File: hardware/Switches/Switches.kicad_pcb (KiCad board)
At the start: 2 copper layers, 22 parts, among them U101 MIC4604YM, U102 MIC4604YM

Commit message: snubber
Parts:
- added C105: 100n, Capacitor_SMD:C_1210_3225Metric_Pad1.33x2.70mm_HandSolder, F.Cu at (129.5, 71.5)
- added C106: 100n, Capacitor_SMD:C_1210_3225Metric_Pad1.33x2.70mm_HandSolder, F.Cu at (128.9, 97.8)
- added C107: 100n, Capacitor_SMD:C_1210_3225Metric_Pad1.33x2.70mm_HandSolder, F.Cu at (202.6, 70.2)
- added C108: 100n, Capacitor_SMD:C_1210_3225Metric_Pad1.33x2.70mm_HandSolder, F.Cu at (203.2, 97.8)
- added R109: 10, Resistor_SMD:R_1210_3225Metric_Pad1.30x2.65mm_HandSolder, F.Cu at (129.5, 65.7)
- added R110: 10, Resistor_SMD:R_1210_3225Metric_Pad1.30x2.65mm_HandSolder, F.Cu at (128.9, 92.4)
- added R111: 10, Resistor_SMD:R_1210_3225Metric_Pad1.30x2.65mm_HandSolder, F.Cu at (202.6, 64.8)
- added R112: 10, Resistor_SMD:R_1210_3225Metric_Pad1.30x2.65mm_HandSolder, F.Cu at (203.2, 92.1)
- moved R102 5.91 mm to (158.1, 81.3)
- moved R101 5.91 mm to (158.1, 78.7)
- moved C103 5.12 mm to (167.5, 84.8)
- moved U101 5.12 mm to (163.0, 84.8)
- moved C101 4.26 mm to (158.1, 83.8), turned to 180 degrees
- moved R105 1.75 mm to (158.2, 86.3)
- moved R106 1.75 mm to (158.2, 88.6)
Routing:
- net /SL1: track 2.07 -> 12.5 mm
- net /GH1_1: track 33.6 -> 28.0 mm
- net Net-(C101-Pad1): track 8.60 -> 5.32 mm
- net Net-(R105-Pad2): track 12.9 -> 9.76 mm
- net /GH1_2: track 20.8 -> 18.5 mm
- net /GL1_1: track 25.2 -> 23.0 mm
- net Net-(U101-Pad6): track 0.00 -> 1.85 mm, vias 0 -> 1
- net Net-(R101-Pad2): track 8.60 -> 7.26 mm
- net /GL1_2: track 33.0 -> 34.2 mm
- net Net-(U101-Pad5): track 0.65 -> 1.80 mm, vias 0 -> 1

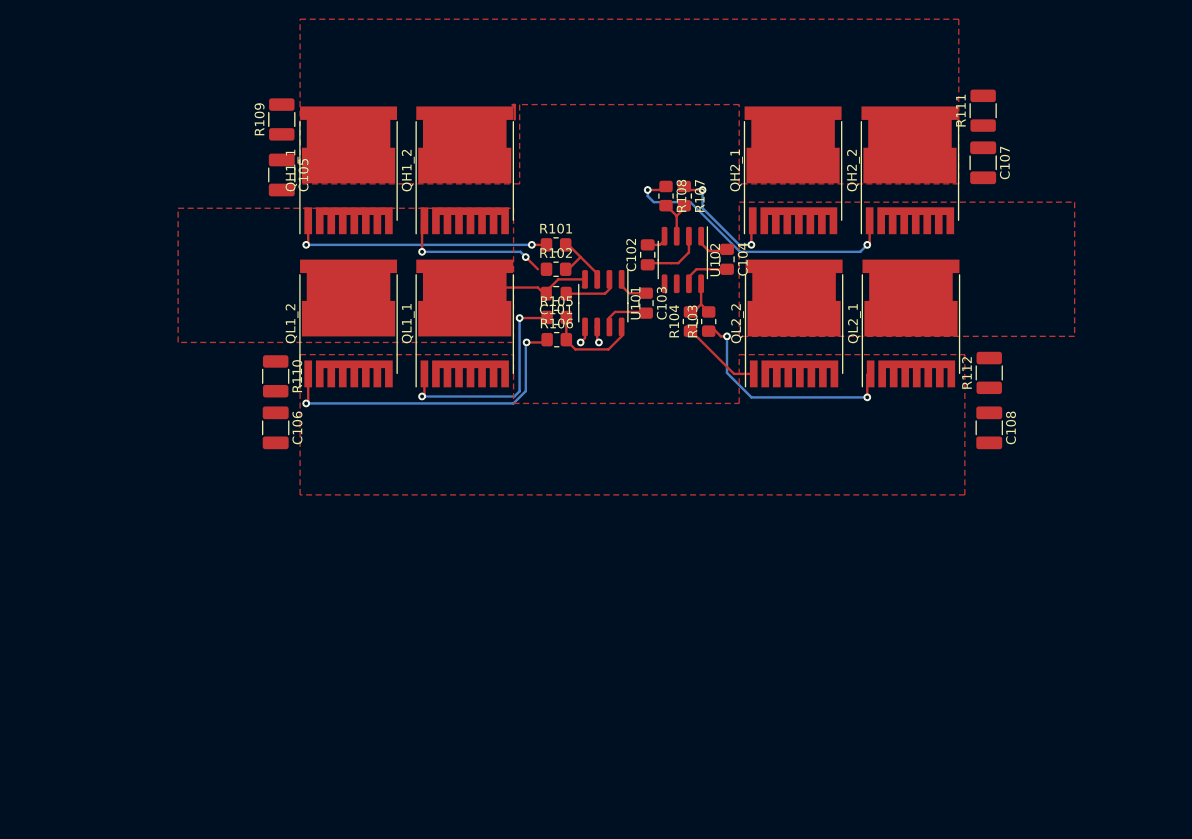
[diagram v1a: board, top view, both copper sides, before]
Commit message: wip: switches pcb routed
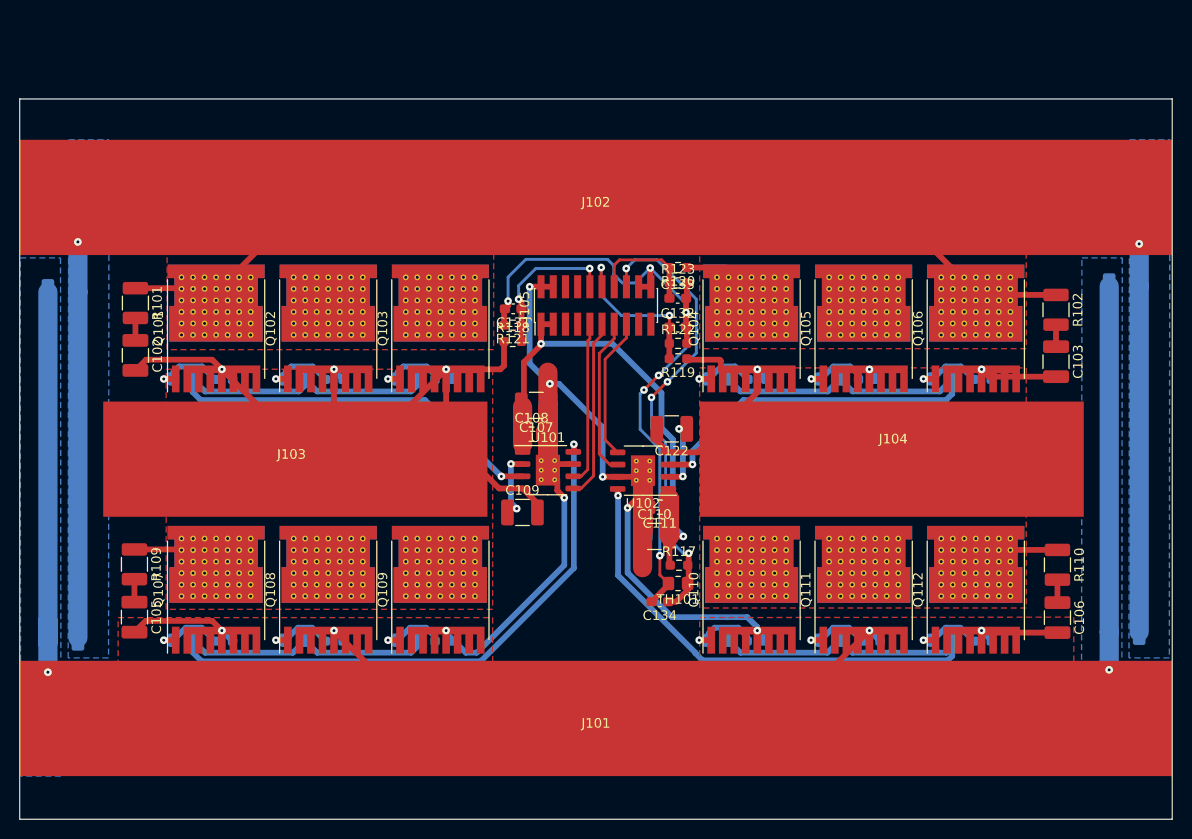
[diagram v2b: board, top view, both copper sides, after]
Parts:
- removed QH1_1, QH1_2, QH2_1, QH2_2, QL1_1, QL1_2, QL2_1, QL2_2: IAUT300N10S5N015, Package_TO_SOT_SMD:Infineon_PG-HSOF-8-1
- added C109: 10uF, Capacitor_SMD:C_1210_3225Metric_Pad1.33x2.70mm_HandSolder, F.Cu at (154.6, 106.6)
- added C110: 10uF, Capacitor_SMD:C_1210_3225Metric_Pad1.33x2.70mm_HandSolder, F.Cu at (168.3, 109.1)
- added C111: 100nF, Capacitor_SMD:C_0805_2012Metric_Pad1.18x1.45mm_HandSolder, F.Cu at (168.9, 106.0)
- added C112: 10u, Capacitor_SMD:C_1210_3225Metric_Pad1.33x2.70mm_HandSolder, B.Cu at (217.2, 119.0)
- added C113: 10u, Capacitor_SMD:C_1210_3225Metric_Pad1.33x2.70mm_HandSolder, B.Cu at (217.2, 115.0)
- added C114: 10u, Capacitor_SMD:C_1210_3225Metric_Pad1.33x2.70mm_HandSolder, B.Cu at (217.2, 111.0)
- added C115: 10u, Capacitor_SMD:C_1210_3225Metric_Pad1.33x2.70mm_HandSolder, B.Cu at (217.2, 107.0)
- added C116: 10u, Capacitor_SMD:C_1210_3225Metric_Pad1.33x2.70mm_HandSolder, B.Cu at (217.2, 103.0)
- added C117: 10u, Capacitor_SMD:C_1210_3225Metric_Pad1.33x2.70mm_HandSolder, B.Cu at (217.2, 99.0)
- added C118: 10u, Capacitor_SMD:C_1210_3225Metric_Pad1.33x2.70mm_HandSolder, B.Cu at (217.2, 95.0)
- added C119: 10u, Capacitor_SMD:C_1210_3225Metric_Pad1.33x2.70mm_HandSolder, B.Cu at (217.2, 91.0)
- added C120: 10u, Capacitor_SMD:C_1210_3225Metric_Pad1.33x2.70mm_HandSolder, B.Cu at (217.2, 87.0)
- added C121: 10u, Capacitor_SMD:C_1210_3225Metric_Pad1.33x2.70mm_HandSolder, B.Cu at (217.2, 83.0)
- added C122: 10uF, Capacitor_SMD:C_1210_3225Metric_Pad1.33x2.70mm_HandSolder, F.Cu at (170.1, 97.9)
- added C123: 10u, Capacitor_SMD:C_1210_3225Metric_Pad1.33x2.70mm_HandSolder, B.Cu at (106.8, 99.7)
- added C124: 10u, Capacitor_SMD:C_1210_3225Metric_Pad1.33x2.70mm_HandSolder, B.Cu at (106.8, 111.7)
- added C125: 10u, Capacitor_SMD:C_1210_3225Metric_Pad1.33x2.70mm_HandSolder, B.Cu at (106.8, 119.7)
- added C126: 10u, Capacitor_SMD:C_1210_3225Metric_Pad1.33x2.70mm_HandSolder, B.Cu at (106.8, 95.7)
- added C127: 10u, Capacitor_SMD:C_1210_3225Metric_Pad1.33x2.70mm_HandSolder, B.Cu at (106.8, 115.7)
- added C128: 10u, Capacitor_SMD:C_1210_3225Metric_Pad1.33x2.70mm_HandSolder, B.Cu at (106.8, 83.7)
- added C129: 10u, Capacitor_SMD:C_1210_3225Metric_Pad1.33x2.70mm_HandSolder, B.Cu at (106.8, 91.7)
- added C130: 10u, Capacitor_SMD:C_1210_3225Metric_Pad1.33x2.70mm_HandSolder, B.Cu at (106.8, 87.7)
- added C131: 1pF, Capacitor_SMD:C_0603_1608Metric_Pad1.08x0.95mm_HandSolder, F.Cu at (153.6, 85.4)
- added C132: 1pF, Capacitor_SMD:C_0603_1608Metric_Pad1.08x0.95mm_HandSolder, F.Cu at (170.8, 87.3)
- added C133: 1pF, Capacitor_SMD:C_0603_1608Metric_Pad1.08x0.95mm_HandSolder, F.Cu at (170.8, 84.3)
- added C134: 100nF, Capacitor_SMD:C_0603_1608Metric_Pad1.08x0.95mm_HandSolder, F.Cu at (168.9, 115.9)
- added J101: BusBar, Switches:BusBar, F.Cu at (162.2, 128.1)
- added J102: BusBar, Switches:BusBar, F.Cu at (162.2, 73.8)
- added J103: BusBar, Switches:BusBar, F.Cu at (130.6, 101.0)
- added J104: BusBar, Switches:BusBar, F.Cu at (193.2, 99.5)
- added J105: Conn_02x03_Odd_Even, Connector_PinHeader_1.27mm:PinHeader_2x10_P1.27mm_Vertical_SMD, F.Cu at (162.2, 85.0)
- added Q101: IPT015N10N5, Package_TO_SOT_SMD:Infineon_PG-HSOF-8-1_ThermalVias, F.Cu at (122.7, 87.5)
- added Q102: IPT015N10N5, Package_TO_SOT_SMD:Infineon_PG-HSOF-8-1_ThermalVias, F.Cu at (134.4, 87.5)
- added Q103: IPT015N10N5, Package_TO_SOT_SMD:Infineon_PG-HSOF-8-1_ThermalVias, F.Cu at (146.1, 87.5)
- added Q104: IPT015N10N5, Package_TO_SOT_SMD:Infineon_PG-HSOF-8-1_ThermalVias, F.Cu at (178.4, 87.5)
- added Q105: IPT015N10N5, Package_TO_SOT_SMD:Infineon_PG-HSOF-8-1_ThermalVias, F.Cu at (190.1, 87.5)
- added Q106: IPT015N10N5, Package_TO_SOT_SMD:Infineon_PG-HSOF-8-1_ThermalVias, F.Cu at (201.8, 87.5)
- added Q107: IPT015N10N5, Package_TO_SOT_SMD:Infineon_PG-HSOF-8-1_ThermalVias, F.Cu at (122.7, 114.7)
- added Q108: IPT015N10N5, Package_TO_SOT_SMD:Infineon_PG-HSOF-8-1_ThermalVias, F.Cu at (134.4, 114.7)
- added Q109: IPT015N10N5, Package_TO_SOT_SMD:Infineon_PG-HSOF-8-1_ThermalVias, F.Cu at (146.1, 114.7)
- added Q110: IPT015N10N5, Package_TO_SOT_SMD:Infineon_PG-HSOF-8-1_ThermalVias, F.Cu at (178.4, 114.7)
- added Q111: IPT015N10N5, Package_TO_SOT_SMD:Infineon_PG-HSOF-8-1_ThermalVias, F.Cu at (190.1, 114.7)
- added Q112: IPT015N10N5, Package_TO_SOT_SMD:Infineon_PG-HSOF-8-1_ThermalVias, F.Cu at (201.8, 114.7)
- added R113: 4R7, Resistor_SMD:R_0805_2012Metric_Pad1.20x1.40mm_HandSolder, B.Cu at (198.3, 92.7)
- added R114: 4R7, Resistor_SMD:R_0805_2012Metric_Pad1.20x1.40mm_HandSolder, B.Cu at (175.0, 119.9)
- added R115: 4R7, Resistor_SMD:R_0805_2012Metric_Pad1.20x1.40mm_HandSolder, B.Cu at (186.7, 119.9)
- added R116: 4R7, Resistor_SMD:R_0805_2012Metric_Pad1.20x1.40mm_HandSolder, B.Cu at (198.3, 119.9)
- added R117: 47k, Resistor_SMD:R_0603_1608Metric_Pad0.98x0.95mm_HandSolder, F.Cu at (170.9, 112.1)
- added R118: 10k, Resistor_SMD:R_0603_1608Metric_Pad0.98x0.95mm_HandSolder, F.Cu at (153.6, 88.8)
- added R119: 10k, Resistor_SMD:R_0603_1608Metric_Pad0.98x0.95mm_HandSolder, F.Cu at (170.8, 90.6)
- added R120: 10k, Resistor_SMD:R_0603_1608Metric_Pad0.98x0.95mm_HandSolder, F.Cu at (170.8, 81.1)
- added R121: 330, Resistor_SMD:R_0603_1608Metric_Pad0.98x0.95mm_HandSolder, F.Cu at (153.6, 87.1)
- added R122: 330, Resistor_SMD:R_0603_1608Metric_Pad0.98x0.95mm_HandSolder, F.Cu at (170.8, 89.0)
- added R123: 330, Resistor_SMD:R_0603_1608Metric_Pad0.98x0.95mm_HandSolder, F.Cu at (170.8, 82.7)
- added R124: 10k, Resistor_SMD:R_0603_1608Metric_Pad0.98x0.95mm_HandSolder, B.Cu at (123.5, 92.8)
- added R125: 10k, Resistor_SMD:R_0603_1608Metric_Pad0.98x0.95mm_HandSolder, B.Cu at (135.0, 92.8)
- added R126: 10k, Resistor_SMD:R_0603_1608Metric_Pad0.98x0.95mm_HandSolder, B.Cu at (146.4, 92.8)
- added R127: 10k, Resistor_SMD:R_0603_1608Metric_Pad0.98x0.95mm_HandSolder, B.Cu at (123.5, 120.0)
- added R128: 10k, Resistor_SMD:R_0603_1608Metric_Pad0.98x0.95mm_HandSolder, B.Cu at (135.0, 120.0)
- added R129: 10k, Resistor_SMD:R_0603_1608Metric_Pad0.98x0.95mm_HandSolder, B.Cu at (146.4, 120.0)
- added R130: 10k, Resistor_SMD:R_0603_1608Metric_Pad0.98x0.95mm_HandSolder, B.Cu at (179.0, 92.8)
- added R131: 10k, Resistor_SMD:R_0603_1608Metric_Pad0.98x0.95mm_HandSolder, B.Cu at (190.5, 92.8)
- added R132: 10k, Resistor_SMD:R_0603_1608Metric_Pad0.98x0.95mm_HandSolder, B.Cu at (202.5, 92.8)
- added R133: 10k, Resistor_SMD:R_0603_1608Metric_Pad0.98x0.95mm_HandSolder, B.Cu at (178.9, 120.0)
- added R134: 10k, Resistor_SMD:R_0603_1608Metric_Pad0.98x0.95mm_HandSolder, B.Cu at (190.9, 120.0)
- added R135: 10k, Resistor_SMD:R_0603_1608Metric_Pad0.98x0.95mm_HandSolder, B.Cu at (202.5, 120.0)
- added TH101: SDNT2012X103F3950FTF, Resistor_SMD:R_0805_2012Metric_Pad1.20x1.40mm_HandSolder, F.Cu at (170.8, 114.0)
- C101, C104: value 100n -> 10u; footprint Capacitor_SMD:C_0805_2012Metric_Pad1.18x1.45mm_HandSolder -> Capacitor_SMD:C_1210_3225Metric_Pad1.33x2.70mm_HandSolder; moved to B.Cu
- C102, C103: footprint Capacitor_SMD:C_0805_2012Metric_Pad1.18x1.45mm_HandSolder -> Capacitor_SMD:C_1210_3225Metric_Pad1.33x2.70mm_HandSolder
- C107: value 100n -> 10uF
- C108: value 100n -> 100nF; footprint Capacitor_SMD:C_1210_3225Metric_Pad1.33x2.70mm_HandSolder -> Capacitor_SMD:C_0805_2012Metric_Pad1.18x1.45mm_HandSolder
- R101, R102: footprint Resistor_SMD:R_0805_2012Metric_Pad1.20x1.40mm_HandSolder -> Resistor_SMD:R_1210_3225Metric_Pad1.30x2.65mm_HandSolder
- R103, R104, R105, R106, R107, R108: value 10 -> 4R7; moved to B.Cu
- R111, R112: value 10 -> 4R7; footprint Resistor_SMD:R_1210_3225Metric_Pad1.30x2.65mm_HandSolder -> Resistor_SMD:R_0805_2012Metric_Pad1.20x1.40mm_HandSolder; moved to B.Cu
- U101, U102: value MIC4604YM -> UCC27211DDAR; footprint Package_SO:SOIC-8_3.9x4.9mm_P1.27mm -> Package_SO:SOIC-8-1EP_3.9x4.9mm_P1.27mm_EP2.514x3.2mm_ThermalVias
- moved C106 83.8 mm to (210.3, 117.5)
- moved R110 83.7 mm to (210.3, 112.0)
- moved C104 74.4 mm to (106.8, 107.7), turned to 180 degrees
- moved R107 61.5 mm to (130.9, 119.9), turned to 0 degrees
- moved R103 55.1 mm to (119.2, 92.7), turned to 0 degrees
- moved C101 55.1 mm to (106.8, 103.7)
- moved C102 54.4 mm to (114.3, 90.2), turned to 270 degrees
- moved R108 53.5 mm to (142.6, 119.9), turned to 0 degrees
- moved C107 52.9 mm to (156.0, 95.5), turned to 180 degrees
- moved R102 52.2 mm to (210.2, 85.5), turned to 270 degrees
- moved R106 49.9 mm to (119.2, 119.9)
- moved R109 48.8 mm to (114.2, 112.0), turned to 270 degrees
- moved C105 48.5 mm to (114.2, 117.5)
- moved C108 47.7 mm to (155.6, 98.5), turned to 0 degrees
- moved R101 44.2 mm to (114.3, 84.8), turned to 270 degrees
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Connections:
- C101 pad 1: Net-(C101-Pad1) -> +BATT
- C101 pad 2: /SL1 -> GND
- C102 pad 2: /SL2 -> /SL1
- C103 pad 1: VCC -> Net-(C103-Pad1)
- C103 pad 2: GND -> /SL2
- C104 pad 1: VCC -> +BATT
- C105 pad 2: /SL1 -> GND
- C107 pad 1: Net-(C107-Pad1) -> GND
- C107 pad 2: /SL2 -> +15V
- C108 pad 1: Net-(C108-Pad1) -> +15V
- R101 pad 1: /GH1_1 -> +BATT
- R101 pad 2: Net-(R101-Pad2) -> Net-(C102-Pad1)
- R102 pad 1: /GH1_2 -> +BATT
- R102 pad 2: Net-(R101-Pad2) -> Net-(C103-Pad1)
- R103 pad 1: /GL2_1 -> /GH1_1
- R104 pad 1: /GL2_2 -> /GH1_2
- R105 pad 1: /GL1_1 -> /GH1_3
- R105 pad 2: Net-(R105-Pad2) -> Net-(R103-Pad2)
- R106 pad 1: /GL1_2 -> /GL1_1
- R106 pad 2: Net-(R105-Pad2) -> Net-(R106-Pad2)
- R107 pad 1: /GH2_1 -> /GL1_2
- R107 pad 2: Net-(R107-Pad2) -> Net-(R106-Pad2)
- R108 pad 1: /GH2_2 -> /GL1_3
- R108 pad 2: Net-(R107-Pad2) -> Net-(R106-Pad2)
- R109 pad 1: Net-(C105-Pad1) -> /SL1
- R109 pad 2: /Vin -> Net-(C105-Pad1)
- R110 pad 1: Net-(C106-Pad1) -> /SL2
- R110 pad 2: /SL1 -> Net-(C106-Pad1)
- R111 pad 1: Net-(C107-Pad1) -> /GH2_1
- R111 pad 2: /Vin -> Net-(R111-Pad2)
- R112 pad 1: Net-(C108-Pad1) -> /GH2_2
- R112 pad 2: /SL2 -> Net-(R111-Pad2)
- U101 pad 1: VCC -> +15V
- U101 pad 2: Net-(C101-Pad1) -> Net-(C109-Pad1)
- U101 pad 3: Net-(R101-Pad2) -> Net-(R103-Pad2)
- U101 pad 5: Net-(U101-Pad5) -> /PWM_H1
- U101 pad 6: Net-(U101-Pad6) -> /PWM_L1
- U101 pad 8: Net-(R105-Pad2) -> Net-(R106-Pad2)
- U102 pad 1: VCC -> +15V
- U102 pad 2: Net-(C102-Pad1) -> Net-(C122-Pad1)
- U102 pad 3: Net-(R107-Pad2) -> Net-(R111-Pad2)
- U102 pad 5: Net-(U102-Pad5) -> /PWM_H2
- U102 pad 6: Net-(U102-Pad6) -> /PWM_L2
- U102 pad 8: Net-(R103-Pad2) -> Net-(R114-Pad2)
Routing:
- net GND: track 9.53 -> 324.2 mm, vias 0 -> 13
- net +BATT: track 0.00 -> 193.7 mm, vias 0 -> 2
- net /SL1: track 12.5 -> 98.5 mm, vias 0 -> 3
- net Net-(R106-Pad2): track 0.00 -> 85.1 mm, vias 0 -> 1
- net GNDA: track 0.00 -> 75.7 mm, vias 0 -> 6
- net Net-(R114-Pad2): track 0.00 -> 75.3 mm, vias 0 -> 1
- net +15V: track 0.00 -> 63.4 mm, vias 0 -> 2
- net Net-(R111-Pad2): track 0.00 -> 60.5 mm, vias 0 -> 1
- net Net-(R103-Pad2): track 5.25 -> 65.7 mm, vias 0 -> 1
- net /TEMP1: track 0.00 -> 48.3 mm, vias 0 -> 4
- net /SL2: track 2.60 -> 46.3 mm, vias 0 -> 3
- net /GL1_2: track 34.2 -> 7.53 mm, vias 2 -> 1
- net /GH2_2: track 31.0 -> 7.54 mm, vias 2 -> 1
- net /GH1_1: track 28.0 -> 8.10 mm, vias 2 -> 1
- net /PWM_H1: track 0.00 -> 18.8 mm
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- added copper zone on B.Cu, net +BATT
- added copper zone on F.Cu, net +BATT
- added copper zone on B.Cu, net GND
- removed copper zone on F.Cu, net /Vin
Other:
- board outline added: 120 x 75 mm
- net class Default: clearance 0.2 -> 0.3; trace_width 0.25 -> 0.3; via_drill 0.4 -> 0.3
- rule trace_clearance: 0.2 -> 0.3
